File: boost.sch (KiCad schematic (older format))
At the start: 14 parts, among them SW1 SW_SPST, U2 TPS61022

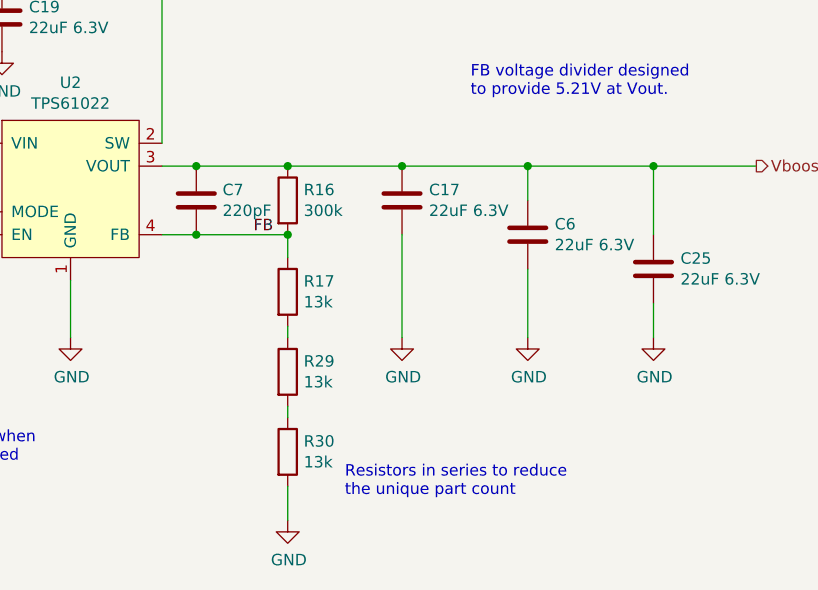
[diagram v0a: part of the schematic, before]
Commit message: Revert back to using INA199 as a current limiter
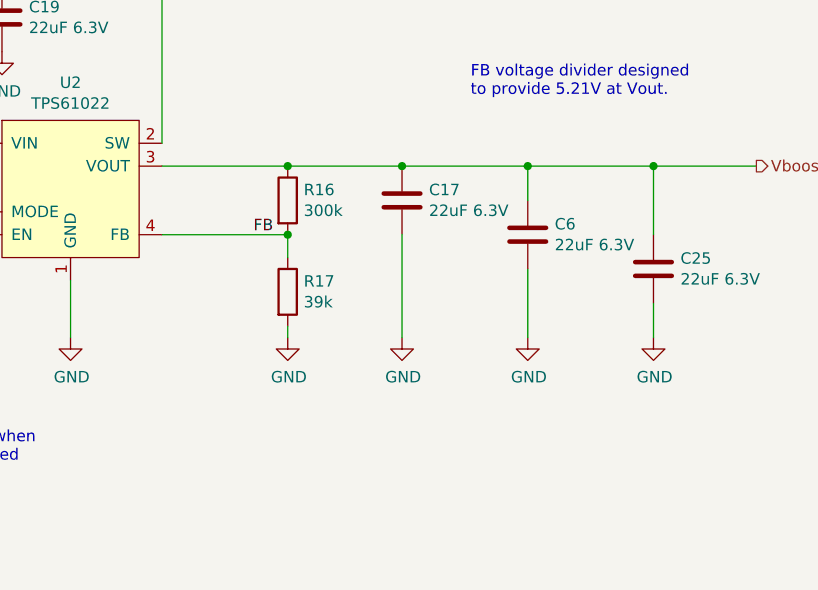
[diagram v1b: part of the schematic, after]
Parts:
- removed C7: 220pF, Capacitor_SMD:C_0603_1608Metric, symbol Device:C
- removed R29, R30: 13k, Resistor_SMD:R_0603_1608Metric, symbol Device:R
- R17: value 13k -> 39k; LCSC C22797 -> C23153
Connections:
- net GND: now also R17.2
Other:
- note removed: "Resistors in series to reduce\nthe unique part count"
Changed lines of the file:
@@
 AR Path="/5CA73F16/5CA6B522" Ref="R17"  Part="1"
 F 0 "R17" H 4420 2896 50  0000 L CNN
-F 1 "13k" H 4420 2805 50  0000 L CNN
+F 1 "39k" H 4420 2805 50  0000 L CNN
 F 2 "Resistor_SMD:R_0603_1608Metric" V 4280 2850 50  0001 C CNN
 F 3 "~" H 4350 2850 50  0001 C CNN
-F 4 "C22797" H 4350 2850 50  0001 C CNN "LCSC"
+F 4 "C23153" H 4350 2850 50  0001 C CNN "LCSC"
 	1    4350 2850
 	1    0    0    -1
@@
 L power:GND #PWR?
 U 1 1 5CA6B529
-P 4350 3850
+P 4350 3050
 AR Path="/5CA6B529" Ref="#PWR?"  Part="1"
 AR Path="/5C3480BB/5CA6B529" Ref="#PWR?"  Part="1"
 AR Path="/5CA73F16/5CA6B529" Ref="#PWR045"  Part="1"
-F 0 "#PWR045" H 4350 3600 50  0001 C CNN
-F 1 "GND" H 4355 3677 50  0000 C CNN
-F 2 "" H 4350 3850 50  0001 C CNN
-F 3 "" H 4350 3850 50  0001 C CNN
-	1    4350 3850
+F 0 "#PWR045" H 4350 2800 50  0001 C CNN
+F 1 "GND" H 4355 2877 50  0000 C CNN
+F 2 "" H 4350 3050 50  0001 C CNN
+F 3 "" H 4350 3050 50  0001 C CNN
+	1    4350 3050
 	1    0    0    -1
 $EndComp
@@
 	4350 2600 4350 2700
 Connection ~ 4350 2600
-Wire Wire Line
-	4350 3850 4350 3700
 Wire Wire Line
 	2150 1500 2400 1500
@@
 Text HLabel 2150 1500 0    50   Input ~ 0
 Vin
-Wire Wire Line
-	3800 2600 3950 2600
 Text Notes 5150 2000 0    50   ~ 0
 FB voltage divider designed\nto provide 5.21V at Vout.
@@
 Wire Wire Line
 	3400 3050 3400 2800
-Wire Wire Line
-	3800 2300 3950 2300
 Connection ~ 4350 2300
 Connection ~ 4850 2300
@@
 Text Notes 1950 1400 0    50   ~ 0
 Vin at max. 2.65V
-Connection ~ 3950 2300
-Wire Wire Line
-	3950 2300 4350 2300
-Connection ~ 3950 2600
-Wire Wire Line
-	3950 2600 4350 2600
-$Comp
-L Device:C C7
-U 1 1 5D913E0F
-P 3950 2450
-F 0 "C7" H 4065 2496 50  0000 L CNN
-F 1 "220pF" H 4065 2405 50  0000 L CNN
-F 2 "Capacitor_SMD:C_0603_1608Metric" H 3988 2300 50  0001 C CNN
-F 3 "~" H 3950 2450 50  0001 C CNN
-F 4 "C1603" H 3950 2450 50  0001 C CNN "LCSC"
-	1    3950 2450
-	1    0    0    -1
-$EndComp
 Wire Wire Line
 	3800 1500 3800 2200
@@
 Wire Wire Line
 	4850 3050 4850 2600
-$Comp
-L Device:R R?
-U 1 1 5F48CB1D
-P 4350 3200
-AR Path="/5F48CB1D" Ref="R?"  Part="1"
-AR Path="/5C3480BB/5F48CB1D" Ref="R?"  Part="1"
-AR Path="/5CA73F16/5F48CB1D" Ref="R29"  Part="1"
-F 0 "R29" H 4420 3246 50  0000 L CNN
-F 1 "13k" H 4420 3155 50  0000 L CNN
-F 2 "Resistor_SMD:R_0603_1608Metric" V 4280 3200 50  0001 C CNN
-F 3 "~" H 4350 3200 50  0001 C CNN
-F 4 "C22797" H 4350 3200 50  0001 C CNN "LCSC"
-	1    4350 3200
-	1    0    0    -1
-$EndComp
-Wire Wire Line
-	4350 3050 4350 3000
-$Comp
-L Device:R R?
-U 1 1 5F48D0EA
-P 4350 3550
-AR Path="/5F48D0EA" Ref="R?"  Part="1"
-AR Path="/5C3480BB/5F48D0EA" Ref="R?"  Part="1"
-AR Path="/5CA73F16/5F48D0EA" Ref="R30"  Part="1"
-F 0 "R30" H 4420 3596 50  0000 L CNN
-F 1 "13k" H 4420 3505 50  0000 L CNN
-F 2 "Resistor_SMD:R_0603_1608Metric" V 4280 3550 50  0001 C CNN
-F 3 "~" H 4350 3550 50  0001 C CNN
-F 4 "C22797" H 4350 3550 50  0001 C CNN "LCSC"
-	1    4350 3550
-	1    0    0    -1
-$EndComp
-Wire Wire Line
-	4350 3400 4350 3350
 Text Notes 900  3000 0    50   ~ 0
 Switch/header allows for\npower-cycling the RPi.
-Text Notes 4600 3750 0    50   ~ 0
-Resistors in series to reduce\nthe unique part count
 Wire Wire Line
 	2150 2600 2600 2600
@@
 Text Notes 2400 3600 0    50   ~ 0
 R21 pulls EN down when\nthe MCU is unpowered
+Wire Wire Line
+	3800 2300 4350 2300
+Wire Wire Line
+	3800 2600 4350 2600
+Wire Wire Line
+	4350 3000 4350 3050
 $EndSCHEMATC

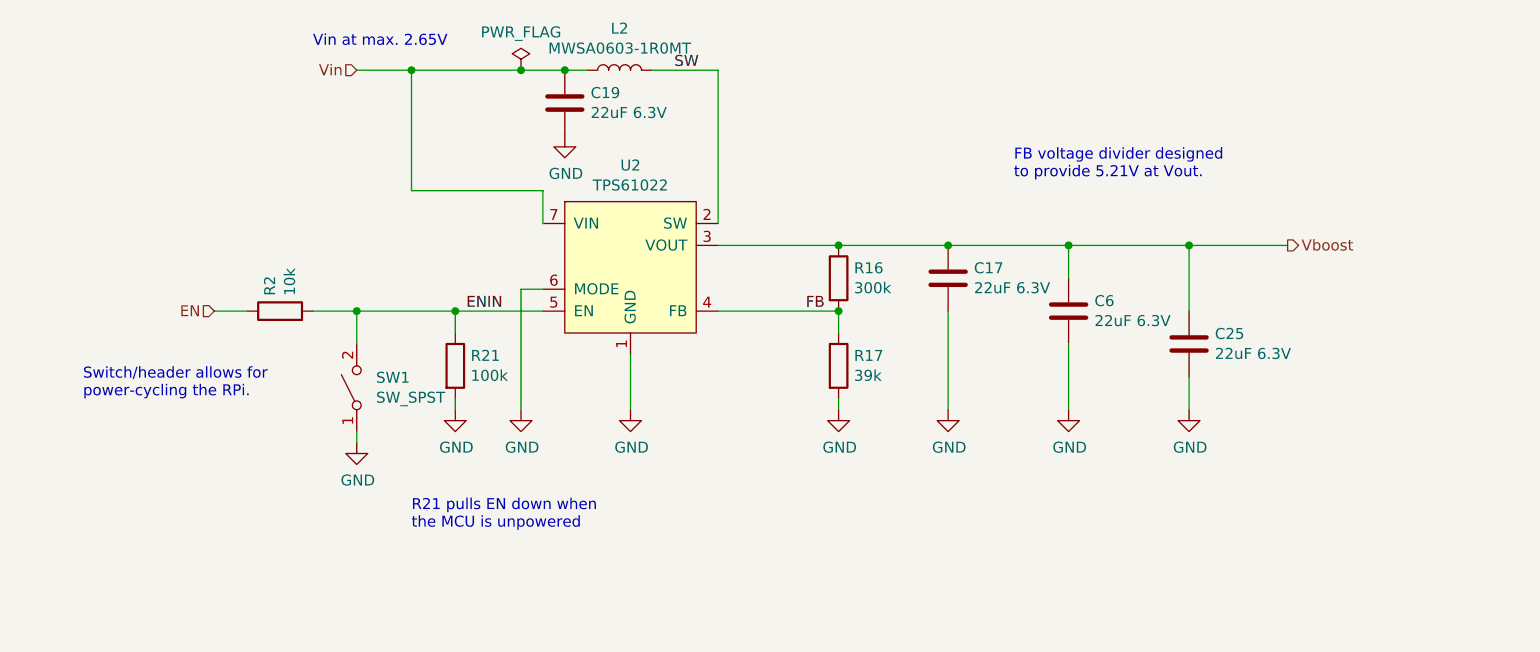
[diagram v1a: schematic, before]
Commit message: Schema updated
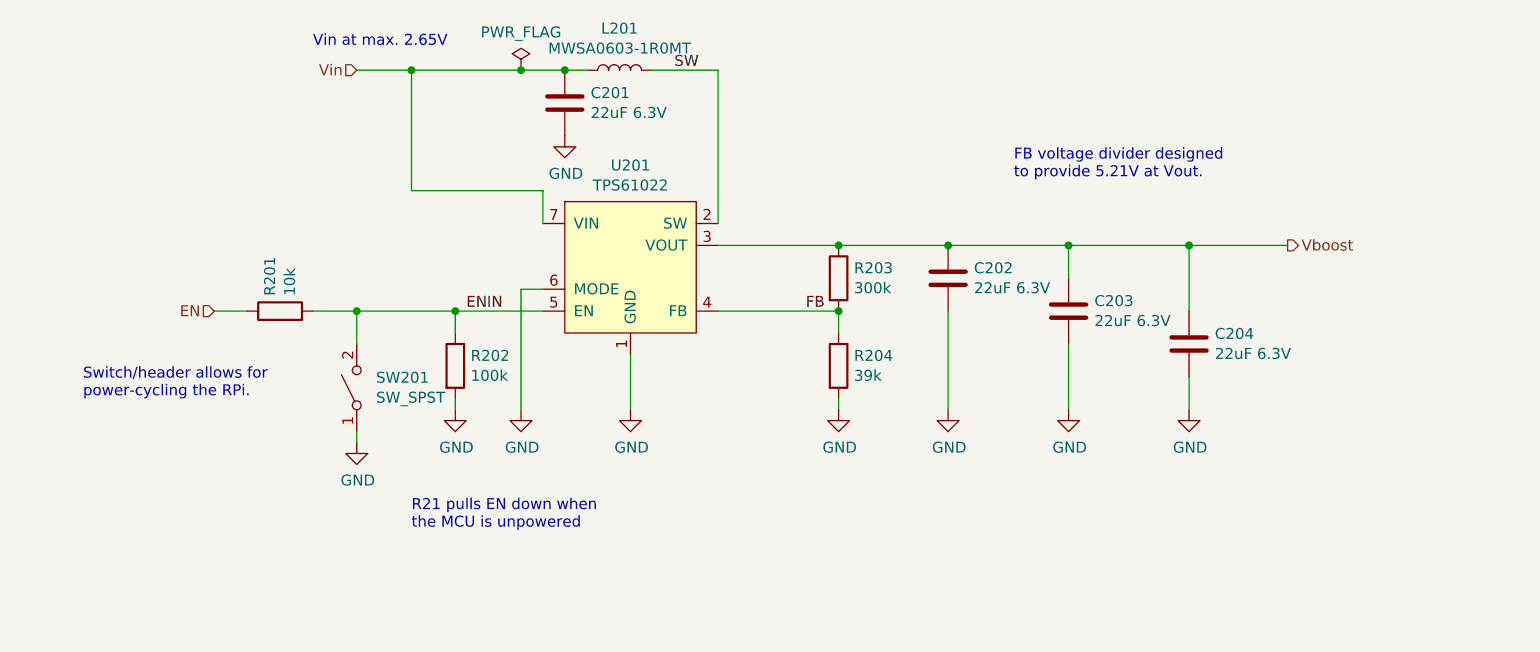
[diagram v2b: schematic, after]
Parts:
- renumbered C19 to C201, C17 to C202, C6 to C203, C25 to C204, L2 to L201, R2 to R201, R21 to R202, R16 to R203, R17 to R204, SW1 to SW201, U2 to U201
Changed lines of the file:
@@
 $Descr A4 11693 8268
 encoding utf-8
-Sheet 3 7
-Title ""
+Sheet 2 8
+Title "Sailor Hat for Raspberry Pi"
 Date ""
-Rev ""
-Comp ""
-Comment1 ""
-Comment2 ""
-Comment3 ""
+Rev "revL"
+Comp "Hat Laboratories"
+Comment1 "https://creativecommons.org/licenses/by-sa/4.0"
+Comment2 "To view a copy of this license, visit "
+Comment3 "Sailor Hat for ESP32 is licensed under CC BY-SA 4.0."
 Comment4 ""
 $EndDescr
@@
 AR Path="/5CA6B4E8" Ref="C?"  Part="1"
 AR Path="/5C3480BB/5CA6B4E8" Ref="C?"  Part="1"
-AR Path="/5CA73F16/5CA6B4E8" Ref="C17"  Part="1"
-F 0 "C17" H 4968 2496 50  0000 L CNN
+AR Path="/5CA73F16/5CA6B4E8" Ref="C202"  Part="1"
+F 0 "C202" H 4968 2496 50  0000 L CNN
 F 1 "22uF 6.3V" H 4968 2405 50  0000 L CNN
 F 2 "Capacitor_SMD:C_0805_2012Metric" H 4888 2300 50  0001 C CNN
@@
 P 3350 1500
 AR Path="/5C3480BB/5CA6B4FC" Ref="L?"  Part="1"
-AR Path="/5CA73F16/5CA6B4FC" Ref="L2"  Part="1"
-F 0 "L2" V 3540 1500 50  0000 C CNN
+AR Path="/5CA73F16/5CA6B4FC" Ref="L201"  Part="1"
+F 0 "L201" V 3540 1500 50  0000 C CNN
 F 1 "MWSA0603-1R0MT" V 3449 1500 50  0000 C CNN
 F 2 "Inductor_SMD:L_Abracon_ASPI-0630LR" H 3350 1500 50  0001 C CNN
@@
 AR Path="/5CA6B51B" Ref="R?"  Part="1"
 AR Path="/5C3480BB/5CA6B51B" Ref="R?"  Part="1"
-AR Path="/5CA73F16/5CA6B51B" Ref="R16"  Part="1"
-F 0 "R16" H 4420 2496 50  0000 L CNN
+AR Path="/5CA73F16/5CA6B51B" Ref="R203"  Part="1"
+F 0 "R203" H 4420 2496 50  0000 L CNN
 F 1 "300k" H 4420 2405 50  0000 L CNN
 F 2 "Resistor_SMD:R_0603_1608Metric" V 4280 2450 50  0001 C CNN
@@
 AR Path="/5CA6B522" Ref="R?"  Part="1"
 AR Path="/5C3480BB/5CA6B522" Ref="R?"  Part="1"
-AR Path="/5CA73F16/5CA6B522" Ref="R17"  Part="1"
-F 0 "R17" H 4420 2896 50  0000 L CNN
+AR Path="/5CA73F16/5CA6B522" Ref="R204"  Part="1"
+F 0 "R204" H 4420 2896 50  0000 L CNN
 F 1 "39k" H 4420 2805 50  0000 L CNN
 F 2 "Resistor_SMD:R_0603_1608Metric" V 4280 2850 50  0001 C CNN
@@
 AR Path="/5CA6B529" Ref="#PWR?"  Part="1"
 AR Path="/5C3480BB/5CA6B529" Ref="#PWR?"  Part="1"
-AR Path="/5CA73F16/5CA6B529" Ref="#PWR045"  Part="1"
-F 0 "#PWR045" H 4350 2800 50  0001 C CNN
+AR Path="/5CA73F16/5CA6B529" Ref="#PWR0206"  Part="1"
+F 0 "#PWR0206" H 4350 2800 50  0001 C CNN
 F 1 "GND" H 4355 2877 50  0000 C CNN
 F 2 "" H 4350 3050 50  0001 C CNN
@@
 AR Path="/5CF608F8" Ref="C?"  Part="1"
 AR Path="/5C3480BB/5CF608F8" Ref="C?"  Part="1"
-AR Path="/5CA73F16/5CF608F8" Ref="C19"  Part="1"
-F 0 "C19" H 3218 1696 50  0000 L CNN
+AR Path="/5CA73F16/5CF608F8" Ref="C201"  Part="1"
+F 0 "C201" H 3218 1696 50  0000 L CNN
 F 1 "22uF 6.3V" H 3218 1605 50  0000 L CNN
 F 2 "Capacitor_SMD:C_0805_2012Metric" H 3138 1500 50  0001 C CNN
@@
 AR Path="/5CF60DAB" Ref="#PWR?"  Part="1"
 AR Path="/5C3480BB/5CF60DAB" Ref="#PWR?"  Part="1"
-AR Path="/5CA73F16/5CF60DAB" Ref="#PWR0104"  Part="1"
-F 0 "#PWR0104" H 3100 1550 50  0001 C CNN
+AR Path="/5CA73F16/5CF60DAB" Ref="#PWR0204"  Part="1"
+F 0 "#PWR0204" H 3100 1550 50  0001 C CNN
 F 1 "GND" H 3105 1627 50  0000 C CNN
 F 2 "" H 3100 1800 50  0001 C CNN
@@
 AR Path="/5D5460DA" Ref="#PWR?"  Part="1"
 AR Path="/5C3480BB/5D5460DA" Ref="#PWR?"  Part="1"
-AR Path="/5CA73F16/5D5460DA" Ref="#PWR0107"  Part="1"
-F 0 "#PWR0107" H 2900 2800 50  0001 C CNN
+AR Path="/5CA73F16/5D5460DA" Ref="#PWR0203"  Part="1"
+F 0 "#PWR0203" H 2900 2800 50  0001 C CNN
 F 1 "GND" H 2905 2877 50  0000 C CNN
 F 2 "" H 2900 3050 50  0001 C CNN
@@
 $EndComp
 $Comp
-L sailor-hat-rescue:TPS61022-sailor-hat U2
+L sailor-hat-rescue:TPS61022-sailor-hat U201
 U 1 1 5D5AC086
 P 3400 2400
-F 0 "U2" H 3400 2865 50  0000 C CNN
+F 0 "U201" H 3400 2865 50  0000 C CNN
 F 1 "TPS61022" H 3400 2774 50  0000 C CNN
 F 2 "custom:TPS61022RWUR" H 3450 2600 50  0001 C CNN
@@
 AR Path="/5CA6B503" Ref="#PWR?"  Part="1"
 AR Path="/5C3480BB/5CA6B503" Ref="#PWR?"  Part="1"
-AR Path="/5CA73F16/5CA6B503" Ref="#PWR044"  Part="1"
-F 0 "#PWR044" H 3400 2800 50  0001 C CNN
+AR Path="/5CA73F16/5CA6B503" Ref="#PWR0205"  Part="1"
+F 0 "#PWR0205" H 3400 2800 50  0001 C CNN
 F 1 "GND" H 3405 2877 50  0000 C CNN
 F 2 "" H 3400 3050 50  0001 C CNN
@@
 	2900 2500 3000 2500
 $Comp
-L Switch:SW_SPST SW1
+L Switch:SW_SPST SW201
 U 1 1 5D5B325B
 P 2150 2950
-F 0 "SW1" V 2196 2862 50  0000 R CNN
+F 0 "SW201" V 2196 2862 50  0000 R CNN
 F 1 "SW_SPST" V 2105 2862 50  0000 R CNN
 F 2 "Connector_PinHeader_2.54mm:PinHeader_1x02_P2.54mm_Vertical" H 2150 2950 50  0001 C CNN
@@
 AR Path="/5D5B16A2" Ref="R?"  Part="1"
 AR Path="/5C3480BB/5D5B16A2" Ref="R?"  Part="1"
-AR Path="/5CA73F16/5D5B16A2" Ref="R2"  Part="1"
-F 0 "R2" H 1870 2646 50  0000 L CNN
+AR Path="/5CA73F16/5D5B16A2" Ref="R201"  Part="1"
+F 0 "R201" H 1870 2646 50  0000 L CNN
 F 1 "10k" H 1870 2555 50  0000 L CNN
 F 2 "Resistor_SMD:R_0603_1608Metric" V 1730 2600 50  0001 C CNN
@@
 AR Path="/5D5B5E50" Ref="#PWR?"  Part="1"
 AR Path="/5C3480BB/5D5B5E50" Ref="#PWR?"  Part="1"
-AR Path="/5CA73F16/5D5B5E50" Ref="#PWR0108"  Part="1"
-F 0 "#PWR0108" H 2150 2950 50  0001 C CNN
+AR Path="/5CA73F16/5D5B5E50" Ref="#PWR0201"  Part="1"
+F 0 "#PWR0201" H 2150 2950 50  0001 C CNN
 F 1 "GND" H 2155 3027 50  0000 C CNN
 F 2 "" H 2150 3200 50  0001 C CNN
@@
 AR Path="/5D8155D9" Ref="C?"  Part="1"
 AR Path="/5C3480BB/5D8155D9" Ref="C?"  Part="1"
-AR Path="/5CA73F16/5D8155D9" Ref="C6"  Part="1"
-F 0 "C6" H 5518 2646 50  0000 L CNN
+AR Path="/5CA73F16/5D8155D9" Ref="C203"  Part="1"
+F 0 "C203" H 5518 2646 50  0000 L CNN
 F 1 "22uF 6.3V" H 5518 2555 50  0000 L CNN
 F 2 "Capacitor_SMD:C_0805_2012Metric" H 5438 2450 50  0001 C CNN
@@
 	3000 2050 3000 2200
 $Comp
-L power:PWR_FLAG #FLG0101
+L power:PWR_FLAG #FLG0201
 U 1 1 5E2AF28D
 P 2900 1500
-F 0 "#FLG0101" H 2900 1575 50  0001 C CNN
+F 0 "#FLG0201" H 2900 1575 50  0001 C CNN
 F 1 "PWR_FLAG" H 2900 1673 50  0000 C CNN
 F 2 "" H 2900 1500 50  0001 C CNN
@@
 AR Path="/5E6767E0" Ref="C?"  Part="1"
 AR Path="/5C3480BB/5E6767E0" Ref="C?"  Part="1"
-AR Path="/5CA73F16/5E6767E0" Ref="C25"  Part="1"
-F 0 "C25" H 6068 2796 50  0000 L CNN
+AR Path="/5CA73F16/5E6767E0" Ref="C204"  Part="1"
+F 0 "C204" H 6068 2796 50  0000 L CNN
 F 1 "22uF 6.3V" H 6068 2705 50  0000 L CNN
 F 2 "Capacitor_SMD:C_0805_2012Metric" H 5988 2600 50  0001 C CNN
@@
 AR Path="/5E6767E6" Ref="#PWR?"  Part="1"
 AR Path="/5C3480BB/5E6767E6" Ref="#PWR?"  Part="1"
-AR Path="/5CA73F16/5E6767E6" Ref="#PWR058"  Part="1"
-F 0 "#PWR058" H 5950 2800 50  0001 C CNN
+AR Path="/5CA73F16/5E6767E6" Ref="#PWR0209"  Part="1"
+F 0 "#PWR0209" H 5950 2800 50  0001 C CNN
 F 1 "GND" H 5955 2877 50  0000 C CNN
 F 2 "" H 5950 3050 50  0001 C CNN
@@
 AR Path="/5D815A89" Ref="#PWR?"  Part="1"
 AR Path="/5C3480BB/5D815A89" Ref="#PWR?"  Part="1"
-AR Path="/5CA73F16/5D815A89" Ref="#PWR024"  Part="1"
-F 0 "#PWR024" H 5400 2800 50  0001 C CNN
+AR Path="/5CA73F16/5D815A89" Ref="#PWR0208"  Part="1"
+F 0 "#PWR0208" H 5400 2800 50  0001 C CNN
 F 1 "GND" H 5405 2877 50  0000 C CNN
 F 2 "" H 5400 3050 50  0001 C CNN
@@
 AR Path="/5CA6B4EF" Ref="#PWR?"  Part="1"
 AR Path="/5C3480BB/5CA6B4EF" Ref="#PWR?"  Part="1"
-AR Path="/5CA73F16/5CA6B4EF" Ref="#PWR046"  Part="1"
-F 0 "#PWR046" H 4850 2800 50  0001 C CNN
+AR Path="/5CA73F16/5CA6B4EF" Ref="#PWR0207"  Part="1"
+F 0 "#PWR0207" H 4850 2800 50  0001 C CNN
 F 1 "GND" H 4855 2877 50  0000 C CNN
 F 2 "" H 4850 3050 50  0001 C CNN
@@
 AR Path="/5F480D4D" Ref="R?"  Part="1"
 AR Path="/5C3480BB/5F480D4D" Ref="R?"  Part="1"
-AR Path="/5CA73F16/5F480D4D" Ref="R21"  Part="1"
-F 0 "R21" H 2670 2896 50  0000 L CNN
+AR Path="/5CA73F16/5F480D4D" Ref="R202"  Part="1"
+F 0 "R202" H 2670 2896 50  0000 L CNN
 F 1 "100k" H 2670 2805 50  0000 L CNN
 F 2 "Resistor_SMD:R_0603_1608Metric" V 2530 2850 50  0001 C CNN
@@
 AR Path="/5F481463" Ref="#PWR?"  Part="1"
 AR Path="/5C3480BB/5F481463" Ref="#PWR?"  Part="1"
-AR Path="/5CA73F16/5F481463" Ref="#PWR07"  Part="1"
-F 0 "#PWR07" H 2600 2800 50  0001 C CNN
+AR Path="/5CA73F16/5F481463" Ref="#PWR0202"  Part="1"
+F 0 "#PWR0202" H 2600 2800 50  0001 C CNN
 F 1 "GND" H 2605 2877 50  0000 C CNN
 F 2 "" H 2600 3050 50  0001 C CNN
